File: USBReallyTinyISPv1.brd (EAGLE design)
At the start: 29.2 x 17.8 mm, 20 parts, among them IC1 ATTINY2313, IC2 74AC125D, Q1 12 MHz, X1 miniUSB-B

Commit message: Getting it ready for printing
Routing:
- net N$3: track 4.48 -> 6.28 mm
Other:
- board text added: "20141012"
- board text removed: "20120316"

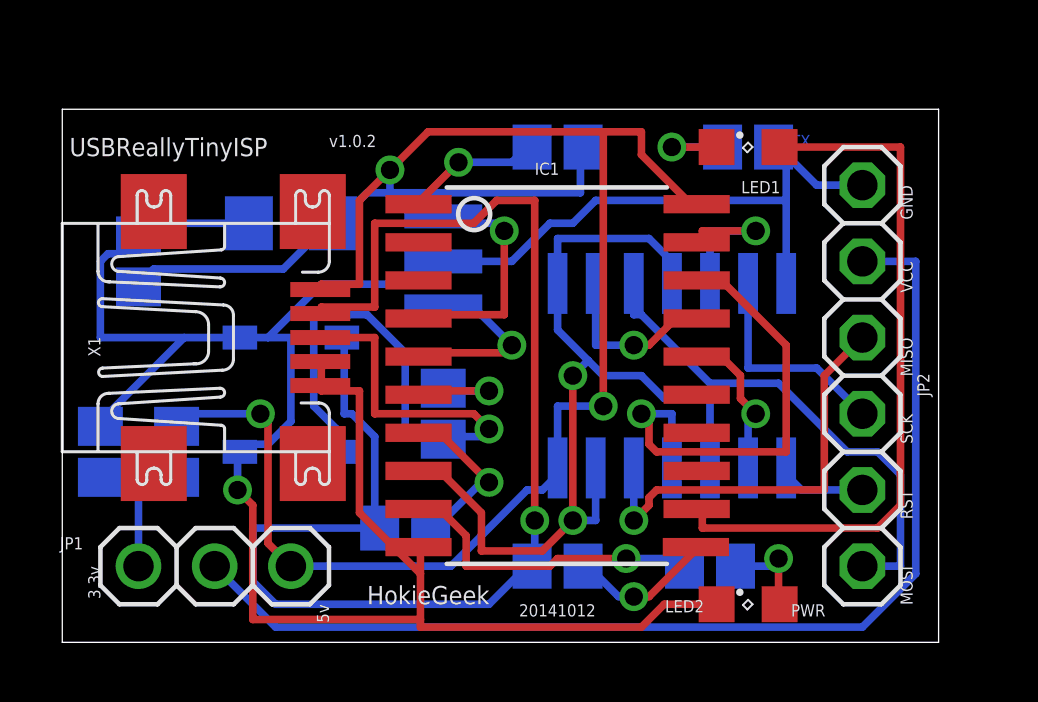
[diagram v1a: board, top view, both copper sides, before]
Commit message: Really rethought the board arrangement and rerouted
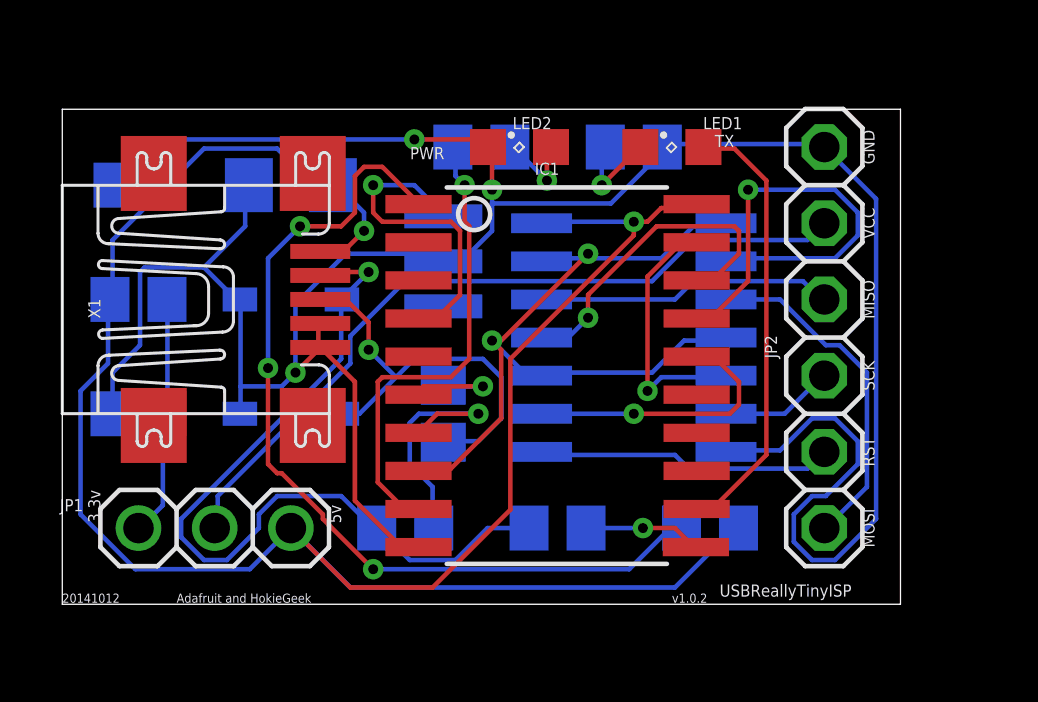
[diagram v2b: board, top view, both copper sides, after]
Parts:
- moved LED2 17.0 mm to (15.2, 16.5)
- moved R2 15.9 mm to (14.0, 16.5)
- moved R6 13.7 mm to (21.6, 3.81)
- moved R7 5.24 mm to (2.54, 11.4), turned to 0 degrees
- moved R1 3.81 mm to (19.1, 16.5)
- moved C1 2.54 mm to (2.54, 15.2), turned to 0 degrees
- moved LED1 2.54 mm to (20.3, 16.5)
- moved JP2 1.80 mm to (25.4, 10.2)
- moved R8 1.80 mm to (2.54, 7.62), turned to 180 degrees
- moved IC2 1.80 mm to (19.1, 10.2), turned to 270 degrees
- moved D2 1.27 mm to (7.62, 7.62)
- moved JP1 1.27 mm to (5.08, 3.81)
- moved R5 1.27 mm to (16.5, 3.81)
- moved C2 1.27 mm to (7.62, 15.2)
- moved D1 1.27 mm to (7.62, 11.4)
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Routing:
- net N$4: track 4.60 -> 30.3 mm, vias 1 -> 3
- net N$11: track 45.9 -> 27.5 mm
- net N$13: track 37.1 -> 25.7 mm
- net GND: track 84.5 -> 93.6 mm, vias 1 -> 3
- net MOSI': track 5.82 -> 14.8 mm
- net N$1: track 23.6 -> 14.8 mm
- net N$10: track 22.8 -> 14.1 mm
- net RST: track 2.98 -> 9.92 mm
- net N$3: track 6.28 -> 0.00 mm, vias 1 -> 0
- net N$12: track 31.7 -> 26.3 mm
- net VCC: track 68.1 -> 73.5 mm, vias 3 -> 2
- net N$5: track 10.5 -> 15.7 mm
- net MOSI: track 16.5 -> 11.5 mm
- net MISO': track 16.0 -> 11.2 mm
- net MISO: track 14.3 -> 9.93 mm, vias 1 -> 0
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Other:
- board size 29.2 x 17.8 mm -> 27.9 x 16.5 mm
- board text added: "Adafruit and HokieGeek"
- board text removed: "HokieGeek"

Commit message: Got my boards back from OSH Park and really need bigger text!
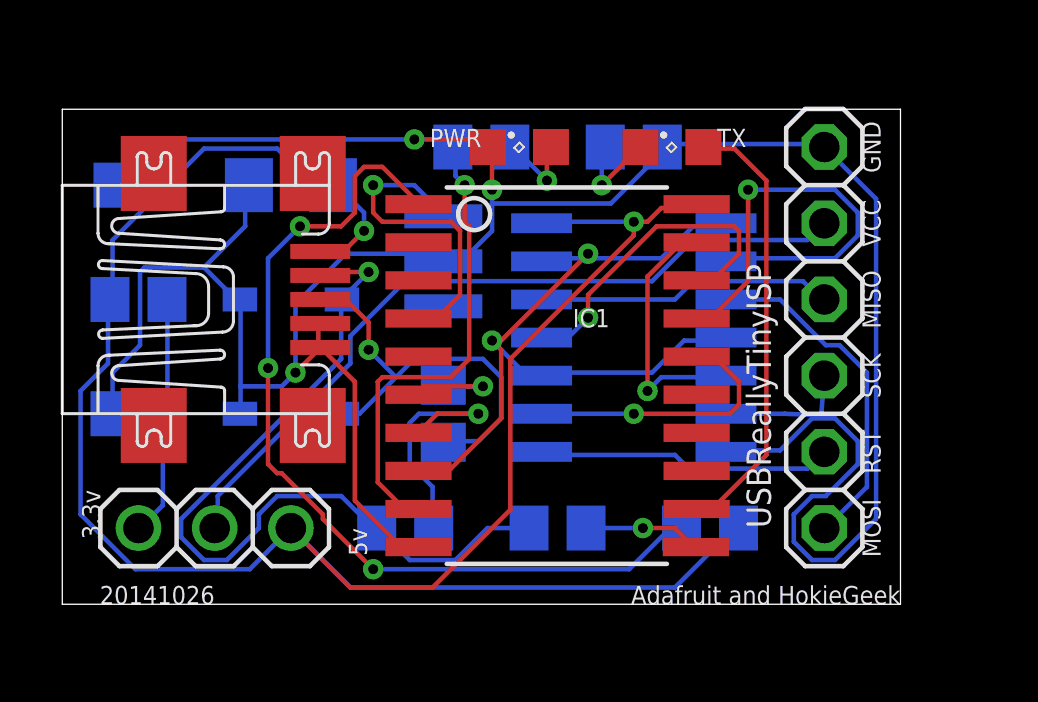
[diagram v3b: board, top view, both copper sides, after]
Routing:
- net SCK: track 3.79 -> 4.50 mm
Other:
- board text added: "20141026"
- board text removed: "20141012"
- board text removed: "v1.0.2"
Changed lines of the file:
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@@
 <wire x1="27.94" y1="17.77" x2="0" y2="17.77" width="0" layer="20"/>
 <wire x1="0" y1="17.77" x2="0" y2="1.27" width="0" layer="20"/>
-<text x="10.16" y="5.08" size="0.4064" layer="22" rot="MR180">47</text>
-<text x="13.97" y="6.35" size="0.4064" layer="22" rot="MR180">47</text>
-<text x="8.89" y="6.35" size="0.4064" layer="22" rot="MR180">3.6v</text>
-<text x="5.08" y="12.7" size="0.4064" layer="22" rot="MR180">3.6v</text>
-<text x="21.59" y="16.51" size="0.4064" layer="22" rot="MR180">1.5k</text>
-<text x="11.43" y="17.78" size="0.4064" layer="22" rot="MR180">1.5k</text>
-<text x="17.78" y="2.54" size="0.4064" layer="22" rot="MR180">1.5k</text>
-<text x="8.89" y="16.51" size="0.4064" layer="22" rot="MR0">100uF</text>
-<text x="11.43" y="15.24" size="0.4064" layer="22" rot="MR270">12Mhz</text>
-<text x="1.27" y="16.51" size="0.4064" layer="22" rot="MR180" align="top-left">0.1uF</text>
-<text x="19.05" y="16.51" size="0.4064" layer="22" rot="MR270">10k</text>
-<text x="2.54" y="8.89" size="0.4064" layer="22" rot="MR180">91k</text>
-<text x="1.27" y="12.7" size="0.4064" layer="22" rot="MR180">47k</text>
-<text x="21.59" y="16.51" size="0.4064" layer="21"> TX</text>
-<text x="11.43" y="16.51" size="0.4064" layer="21" rot="R180" align="bottom-right"> PWR </text>
-<text x="26.67" y="16.51" size="0.4064" layer="21" rot="R270" align="bottom-center">GND </text>
-<text x="26.67" y="13.97" size="0.4064" layer="21" rot="R270" align="bottom-center">VCC </text>
-<text x="26.67" y="11.43" size="0.4064" layer="21" rot="R270" align="bottom-center">MISO </text>
-<text x="26.67" y="8.89" size="0.4064" layer="21" rot="R270" align="bottom-center">SCK </text>
-<text x="26.67" y="6.35" size="0.4064" layer="21" rot="R270" align="bottom-center">RST </text>
-<text x="26.67" y="3.81" size="0.4064" layer="21" rot="R270" align="bottom-center">MOSI </text>
-<text x="1.27" y="5.08" size="0.4064" layer="21" rot="R90" align="bottom-right">3.3v  </text>
-<text x="8.89" y="3.81" size="0.4064" layer="21" rot="R270" align="bottom-right"> 5v</text>
-<text x="21.59" y="2.54" size="0.4064" layer="21" align="top-left">
-  USBReallyTinyISP</text>
-<text x="20.32" y="2.54" size="0.3048" layer="21" align="top-left">
-v1.0.2</text>
-<text x="3.81" y="2.54" size="0.3048" layer="21" align="top-left">
+<text x="10.16" y="5.08" size="0.6096" layer="22" rot="MR0">47</text>
+<text x="11.43" y="7.62" size="0.6096" layer="22" rot="MR270">47</text>
+<text x="7.62" y="8.89" size="0.6096" layer="22" rot="MR0">3.6v</text>
+<text x="7.62" y="12.7" size="0.6096" layer="22" rot="MR0">3.6v</text>
+<text x="21.59" y="16.51" size="0.6096" layer="22" rot="MR180">1.5k</text>
+<text x="10.16" y="16.51" size="0.6096" layer="22" rot="MR180">1.5k</text>
+<text x="16.51" y="5.08" size="0.6096" layer="22" rot="MR0">1.5k</text>
+<text x="7.62" y="16.51" size="0.6096" layer="22" rot="MR0">100uF</text>
+<text x="11.43" y="13.97" size="0.6096" layer="22" rot="MR270">12Mhz</text>
+<text x="1.27" y="16.51" size="0.6096" layer="22" rot="MR180" align="top-left">0.1uF</text>
+<text x="22.86" y="5.08" size="0.6096" layer="22" rot="MR0">10k</text>
+<text x="2.54" y="8.89" size="0.6096" layer="22" rot="MR0">91k</text>
+<text x="2.54" y="12.7" size="0.6096" layer="22" rot="MR0">47k</text>
+<text x="21.59" y="16.51" size="0.6096" layer="21"> TX</text>
+<text x="13.97" y="16.51" size="0.6096" layer="21" align="bottom-right"> PWR </text>
+<text x="26.67" y="16.51" size="0.6096" layer="21" rot="R270" align="bottom-center">GND </text>
+<text x="26.67" y="13.97" size="0.6096" layer="21" rot="R270" align="bottom-center">VCC </text>
+<text x="26.67" y="11.43" size="0.6096" layer="21" rot="R270" align="bottom-center">MISO </text>
+<text x="26.67" y="8.89" size="0.6096" layer="21" rot="R270" align="bottom-center">SCK </text>
+<text x="26.67" y="6.35" size="0.6096" layer="21" rot="R270" align="bottom-center">RST </text>
+<text x="26.67" y="3.81" size="0.6096" layer="21" rot="R270" align="bottom-center">MOSI </text>
+<text x="1.27" y="5.08" size="0.6096" layer="21" rot="R90" align="bottom-right">3.3v</text>
+<text x="10.16" y="3.81" size="0.6096" layer="21" rot="R90" align="bottom-right">
+5v</text>
+<text x="21.59" y="3.81" size="0.8128" layer="21" rot="R90" align="top-left">
+USBReallyTinyISP</text>
+<text x="27.94" y="1.27" size="0.6096" layer="21" rot="R180" align="top-left">
 Adafruit and HokieGeek</text>
-<text x="0" y="2.54" size="0.3048" layer="21" rot="R180" align="bottom-right">
-20141012</text>
+<text x="5.08" y="1.27" size="0.6096" layer="21" align="bottom-right">20141026</text>
 </plain>
 <attributes>
@@
 <attribute name="MF" value="" x="-3.81" y="43.18" size="1.778" layer="28" rot="MR90" display="off"/>
 <attribute name="OC_FARNELL" value="1170434" x="-3.81" y="43.18" size="1.778" layer="28" rot="MR90" display="off"/>
-<attribute name="NAME" x="14.224" y="10.16" size="0.4064" layer="26" rot="MR90"/>
 <attribute name="VALUE" x="9.906" y="10.16" size="1.27" layer="28" rot="MR90"/>
 </element>
 <element name="R1" library="resistor" package="R0805" value="1.5K" x="19.05" y="16.51" smashed="yes" rot="MR0">
-<attribute name="NAME" x="17.272" y="14.986" size="0.4064" layer="26" rot="MR0"/>
+<attribute name="NAME" x="17.272" y="16.256" size="0.4064" layer="26" rot="MR0"/>
 <attribute name="VALUE" x="19.812" y="14.224" size="1.27" layer="28" rot="MR0"/>
 </element>
 <element name="R2" library="resistor" package="R0805" value="1.5K" x="13.97" y="16.51" smashed="yes" rot="MR0">
-<attribute name="NAME" x="14.732" y="17.526" size="0.4064" layer="26" rot="MR0"/>
+<attribute name="NAME" x="16.002" y="16.256" size="0.4064" layer="26" rot="MR0"/>
 <attribute name="VALUE" x="14.732" y="14.224" size="1.27" layer="28" rot="MR0"/>
 </element>
 <element name="R3" library="resistor" package="R0805" value="47" x="12.7" y="7.62" smashed="yes" rot="MR90">
-<attribute name="NAME" x="13.716" y="6.858" size="0.4064" layer="26" rot="MR90"/>
+<attribute name="NAME" x="13.716" y="9.398" size="0.4064" layer="26" rot="MR90"/>
 <attribute name="VALUE" x="10.414" y="6.858" size="1.27" layer="28" rot="MR90"/>
 </element>
@@
 </element>
 <element name="IC1" library="avr-7" package="SO20L$" value="ATTINY2313" x="16.51" y="8.89" smashed="yes" rot="R270">
-<attribute name="NAME" x="15.748" y="15.5829" size="0.4064" layer="25" ratio="10"/>
+<attribute name="NAME" x="17.018" y="10.5029" size="0.6096" layer="25" ratio="10"/>
 <attribute name="VALUE" x="15.3289" y="13.97" size="1.778" layer="27" ratio="10" rot="R270"/>
 </element>
@@
 <attribute name="MF" value="" x="25.4" y="3.81" size="1.778" layer="27" display="off"/>
 <attribute name="OC_FARNELL" value="unknown" x="25.4" y="3.81" size="1.778" layer="27" display="off"/>
-<attribute name="NAME" x="1.27" y="10.795" size="0.4064" layer="25" rot="R90"/>
 <attribute name="VALUE" x="1.905" y="4.445" size="1.27" layer="27"/>
 </element>
 <element name="C1" library="adafruit" package="C0805" value="0.1uF" x="2.54" y="15.24" smashed="yes" rot="MR0">
-<attribute name="NAME" x="3.429" y="16.256" size="0.4064" layer="26" rot="MR0"/>
 <attribute name="VALUE" x="3.429" y="12.954" size="1.27" layer="28" rot="MR0"/>
 </element>
 <element name="LED1" library="led" package="SML0805" value="" x="20.32" y="16.51" smashed="yes">
-<attribute name="NAME" x="21.36" y="17.51" size="0.4064" layer="25" align="top-left"/>
 <attribute name="VALUE" x="18.82" y="14.51" size="1.27" layer="27"/>
 </element>
 <element name="LED2" library="led" package="SML0805" value="" x="15.24" y="16.51" smashed="yes">
-<attribute name="NAME" x="15.01" y="17.51" size="0.4064" layer="25" align="top-left"/>
 <attribute name="VALUE" x="13.74" y="14.51" size="1.27" layer="27"/>
 </element>
 <element name="C2" library="resistor" package="C1206" value="100uF" x="7.62" y="15.24" smashed="yes" rot="MR0">
-<attribute name="NAME" x="8.89" y="16.383" size="0.4064" layer="26" rot="MR0"/>
 <attribute name="VALUE" x="8.89" y="12.827" size="1.27" layer="28" rot="MR0"/>
 </element>
@@
 </element>
 <element name="JP2" library="adafruit" package="1X06" value="" x="25.4" y="10.16" smashed="yes" rot="R270">
-<attribute name="NAME" x="23.4188" y="10.2362" size="0.4064" layer="25" ratio="10" rot="R270"/>
 <attribute name="VALUE" x="22.225" y="17.78" size="1.27" layer="27" rot="R270"/>
 </element>
 <element name="JP1" library="adafruit" package="1X03" value="" x="5.08" y="3.81" smashed="yes">
-<attribute name="NAME" x="-0.0762" y="4.3688" size="0.4064" layer="25" ratio="10"/>
 <attribute name="VALUE" x="1.27" y="0.635" size="1.27" layer="27"/>
 </element>
@@
 <contactref element="JP2" pad="4"/>
 <wire x1="24.0792" y1="7.62" x2="22.1234" y2="7.62" width="0.1524" layer="16"/>
-<wire x1="25.2984" y1="8.8392" x2="24.0792" y2="7.62" width="0.1524" layer="16"/>
-<wire x1="25.2984" y1="8.8392" x2="25.4" y2="8.89" width="0.1524" layer="16"/>
+<wire x1="25.2984" y1="7.5692" x2="24.0792" y2="7.62" width="0.1524" layer="16"/>
+<wire x1="25.2984" y1="7.5692" x2="25.4" y2="8.89" width="0.1524" layer="16"/>
 </signal>
 <signal name="RST">
